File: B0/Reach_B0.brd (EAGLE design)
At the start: 107.3 x 69.5 mm, 185 parts, among them IC1 TMC2100-LA, IC10 74AHC1G126DCK, IC11 74AHC1G126DCK, IC18 74AHC1G126DCK, IC2 TMC2100-LA, IC3 74AHC1G126DCK, IC4 74AHC1G126DCK, IC5 74AHC1G126DCK, IC6 74AHC1G126DCK, IC7 74AHC1G126DCK, IC8 TMC2100-LA, IC9 74AHC1G126DCK, P8 F-2X23-, P9 F-2X23-, Q2 AON6758, Q3 AON6758, U1 SN74AHC595PW, U10 RT8268, U11 PCA9685PW, U18 CAT24C256, U2 SN74AHC595PW, U3 MCP9600, U4 MCP9600, U5 MCP9600, U6 MCP9600, U7 SN74AHC595PW, X1 22-05-7028-02, X11 22-05-7028-02, X14 22-05-7048-04, X2 MSTBA4, X21 MSTBA2, X3 MSTBA2, X4 22-05-7028-02, X5 22-05-7028-02, X6 22-05-7048-04, X7 22-05-7028-02, X8 22-05-7048-04, X9 22-05-7028-02

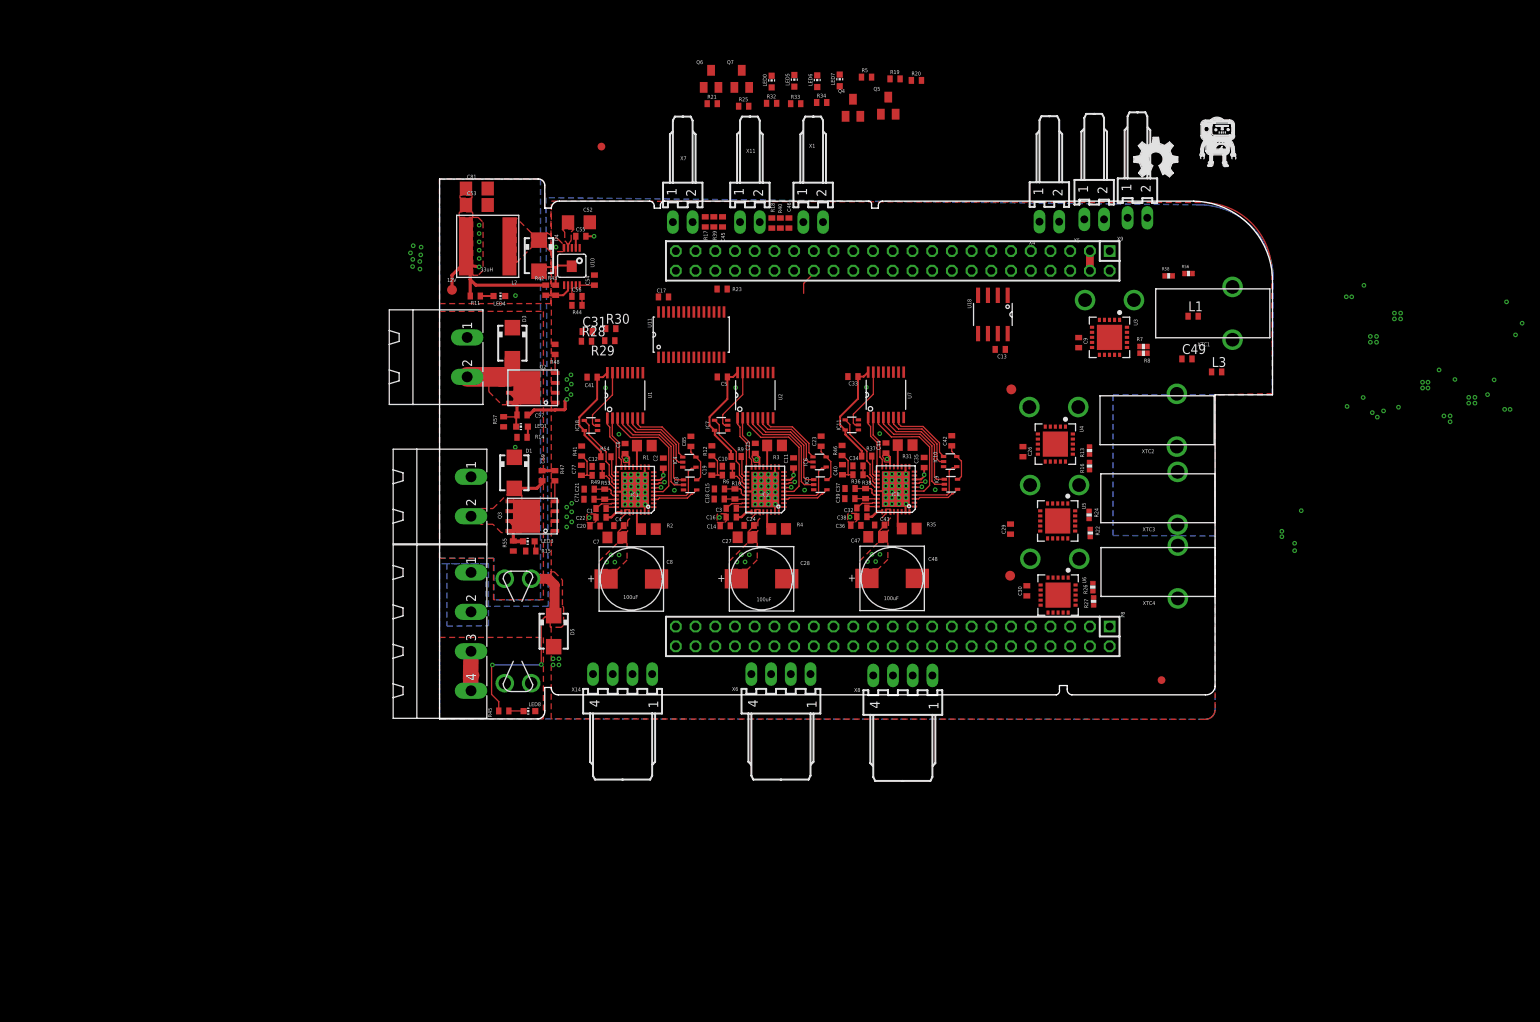
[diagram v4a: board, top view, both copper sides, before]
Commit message: thermocouple layout complete
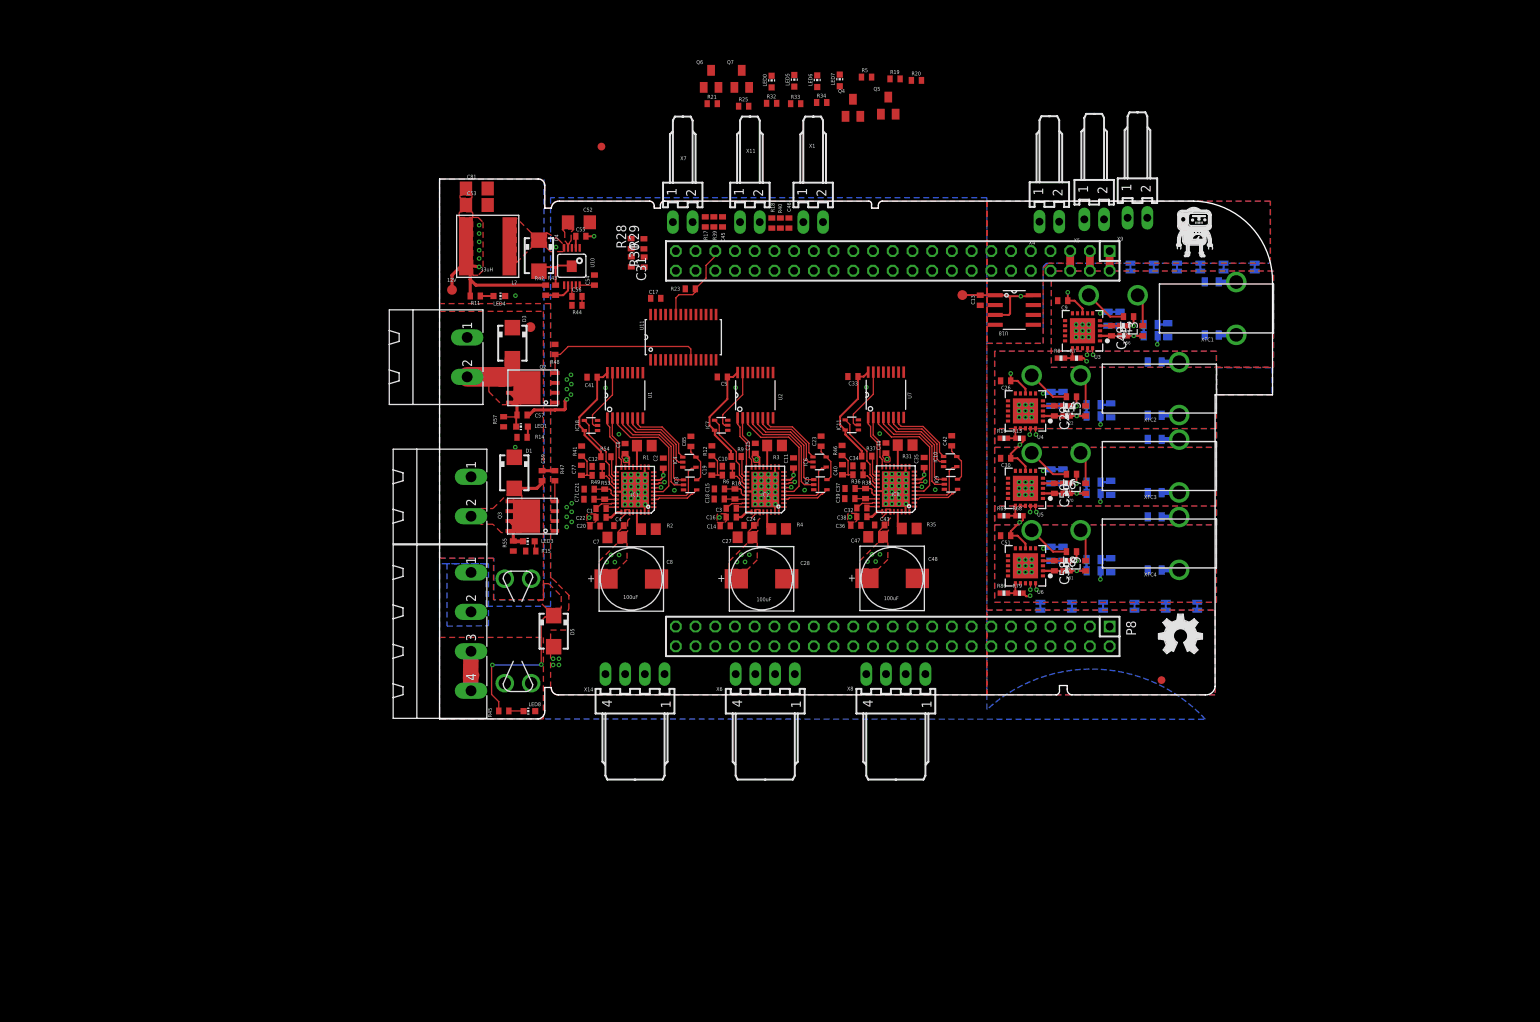
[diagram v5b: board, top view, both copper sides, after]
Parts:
- added C50, C51, C58: 0.1uF, rcl:C0402
- added JP10, JP11, JP12, JP13, JP14, JP3, JP4, JP5, JP6, JP7, JP8, JP9: (no value), SparkFun-PassivesNEW:PAD-JUMPER-2-NC_BY_TRACE_YES_SILK
- added L4, L5, L6, L7, L8, L9: BLM15HB121SN1, inductors:0402
- added R50, R51, R52, R59, R60, R63, R64, R65, R72, R73, R74, R75, R76, R83, R84, R85, R86, R87: 10k, SparkFun-Resistors:0805
- added R61, R62, R66, R67, R77, R78, R88, R89: 0, SparkFun-Resistors:0805
- added R68, R79: 10k, SparkFun-Resistors:0402-RES
- added R69: 4.3k, SparkFun-Resistors:0402-RES
- added R70, R71, R81, R82: 100, SparkFun-Resistors:0402-RES
- added R80: 7.5k, SparkFun-Resistors:0402-RES
- R22: value 10k -> 100
- R24: value 4.3k -> 100
- R26: device SparkFun-Resistors:0402-RES -> SparkFun-Resistors:0805
- R27: value 7.5k -> 10k; device SparkFun-Resistors:0402-RES -> SparkFun-Resistors:0805
- moved 12..24V 69.6 mm to (11.7, 50.5)
- moved LOGO1 61.5 mm to (92.6, 8.41)
- moved R27 26.4 mm to (80.3, 41.2), flipped to the bottom
- moved R26 24.8 mm to (78.8, 41.2), flipped to the bottom, turned to 270 degrees
- moved C30 17.3 mm to (72.9, 33.6), turned to 180 degrees
- moved C29 16.2 mm to (79.2, 39.7), turned to 270 degrees
- moved R22 15.4 mm to (80.8, 39.0), turned to 180 degrees
- moved R24 14.4 mm to (80.7, 40.3), turned to 180 degrees
- moved R28 13.8 mm to (24.7, 61.2), turned to 90 degrees
- moved 3.3V 13.7 mm to (67.3, 54.6)
- moved R29 13.2 mm to (26.3, 61.2), turned to 90 degrees
- moved U$1 12.0 mm to (96.8, 62.8)
- moved R16 11.6 mm to (72.7, 36.1), turned to 0 degrees
- moved R56 11.6 mm to (88.1, 49.4), turned to 180 degrees
- moved L3 10.9 mm to (90.6, 50.0), turned to 90 degrees
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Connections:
- removed net N$41 (its old number): U4.P$4, XTC2.P$4
- new net ENABLE_B: IC2.22, IC7.4
- new net GNDI: C26.2, C30.2, C51.2, C9.2, JP10.2, JP11.2, JP12.2, JP13.2, JP14.2, JP3.2, JP4.2, JP5.2, JP6.2, JP7.2, JP8.2, JP9.2, R16.1, R26.2, R50.2, R60.1, R61.1, R62.1, R65.1, R66.1, R67.1, R69.1, R72.2, R76.1, R77.1, R78.1, R8.1, R80.1, R83.2, R87.1, R88.1, R89.1, U3.P$1, U3.P$10, U3.P$13, U3.P$17, U3.P$18, U3.P$21, U3.P$3, U3.P$5, U3.P$6, U3.P$7, U3.P$9, U4.P$1, U4.P$10, U4.P$13, U4.P$17, U4.P$18, U4.P$21, U4.P$3, U4.P$5, U4.P$6, U4.P$7, U4.P$9, U5.P$1, U5.P$10, U5.P$13, U5.P$17, U5.P$18, U5.P$21, U5.P$3, U5.P$5, U5.P$6, U5.P$7, U5.P$9, U6.P$1, U6.P$10, U6.P$13, U6.P$17, U6.P$18, U6.P$21, U6.P$3, U6.P$5, U6.P$6, U6.P$7, U6.P$9
- new net N$123: L8.2, XTC4.P$4
- new net N$124: R79.1, R80.2, U6.P$16
- new net N$125: L9.1, R81.1, R85.2, R86.2
- new net N$126: C58.2, R81.2, U6.P$2
- new net N$128: C58.1, R82.2, U6.P$4
- new net N$130: L9.2, XTC4.P$3
- new net N$131: L8.1, R82.1, R84.1
- new net N$132: R83.1, R84.2
- new net N$133: R86.1, R87.2
- new net N$134: R88.2, XTC4.P$1
- new net N$135: R89.2, XTC4.P$2
- new net N$42: L5.1, R22.1, R63.2, R64.2
- new net N$51: R61.2, XTC1.P$1
- new net N$73: R62.2, XTC1.P$2
- new net N$75: R59.1, R60.2
- new net N$76: R66.2, XTC2.P$1
- new net N$77: R67.2, XTC2.P$2
- new net N$87: L6.2, XTC3.P$4
- new net N$88: R68.1, R69.2, U5.P$16
- new net N$89: L7.1, R70.1, R74.2, R75.2
- new net N$9: R50.1, R51.2
- new net N$90: C50.2, R70.2, U5.P$2
- new net N$91: C50.1, R71.2, U5.P$4
- new net N$92: L7.2, XTC3.P$3
- new net N$93: L6.1, R71.1, R73.1
- new net N$94: R72.1, R73.2
- new net N$95: R75.1, R76.2
- new net N$97: R77.2, XTC3.P$1
- new net N$98: R78.2, XTC3.P$2
- net +3V3: now also C51.1, R52.1, R63.1, R68.2, R74.1, R79.2, R85.1; no longer C29.1, R22.2, R26.2
- net ENABLE_A: no longer IC2.22, IC7.4
- net GND: now also JP10.1, JP11.1, JP12.1, JP13.1, JP14.1, JP3.1, JP4.1, JP5.1, JP6.1, JP7.1, JP8.1, JP9.1; no longer C26.2, C29.2, C30.2, C9.2, R16.1, R24.1, R27.1, R8.1, U3.P$1, U3.P$10, U3.P$13, U3.P$17, U3.P$18, U3.P$21, U3.P$3, U3.P$5, U3.P$6, U3.P$7, U3.P$9, U4.P$1, U4.P$10, U4.P$13, U4.P$17, U4.P$18, U4.P$21, U4.P$3, U4.P$5, U4.P$6, U4.P$7, U4.P$9, U5.P$1, U5.P$10, U5.P$13, U5.P$17, U5.P$18, U5.P$21, U5.P$3, U5.P$5, U5.P$6, U5.P$7, U5.P$9, U6.P$1, U6.P$10, U6.P$13, U6.P$17, U6.P$18, U6.P$21, U6.P$3, U6.P$5, U6.P$6, U6.P$7, U6.P$9
- net N$11: now also R52.2, R59.2
- net N$38: now also L4.2, XTC2.P$4; no longer U4.P$2, XTC2.P$3
- net N$45: now also C29.2, R22.2, U4.P$2; no longer U5.P$2, XTC3.P$3
- net N$46: now also C29.1, R24.2, U4.P$4; no longer U5.P$4, XTC3.P$4
- net N$47: now also L5.2, XTC2.P$3; no longer R22.1, R24.2, U5.P$16
- net N$48: now also L4.1, R24.1, R27.1; no longer U6.P$2, XTC4.P$3
- net N$49: now also R26.1, R27.2; no longer U6.P$4, XTC4.P$4
- net N$50: now also R64.1, R65.2; no longer R26.1, R27.2, U6.P$16
- net N$72: now also R51.1
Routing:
- net +3V3: track 67.2 -> 274.9 mm, vias 3 -> 14
- net I2C2_SCL: track 0.00 -> 41.4 mm, vias 0 -> 4
- net I2C2_SDA: track 0.00 -> 39.0 mm, vias 0 -> 4
- net HEATER_B: track 2.41 -> 21.9 mm
- net ENABLE: track 0.00 -> 11.3 mm
- net ENABLE_B: track 0.00 -> 10.1 mm
- net ENABLE_A: track 20.1 -> 10.1 mm
- net VDD_IN: track 33.5 -> 24.5 mm, vias 23 -> 21
- net N$87: track 0.00 -> 5.61 mm
- net N$38: track 0.00 -> 5.61 mm
- net N$15: track 0.00 -> 5.61 mm
- net N$123: track 0.00 -> 5.61 mm
- net N$11: track 0.00 -> 4.67 mm, vias 0 -> 1
- net N$42: track 0.00 -> 4.67 mm, vias 0 -> 1
- net N$89: track 0.00 -> 4.67 mm, vias 0 -> 1
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- added copper zone on layer 1, net GNDI
- added copper zone on layer 16, net GNDI
- added copper zone on layer 2, net GNDI
- added copper zone on layer 3, net GNDI
- removed copper zone on layer 1, net N$74
- removed copper zone on layer 3, net VDD_ADC

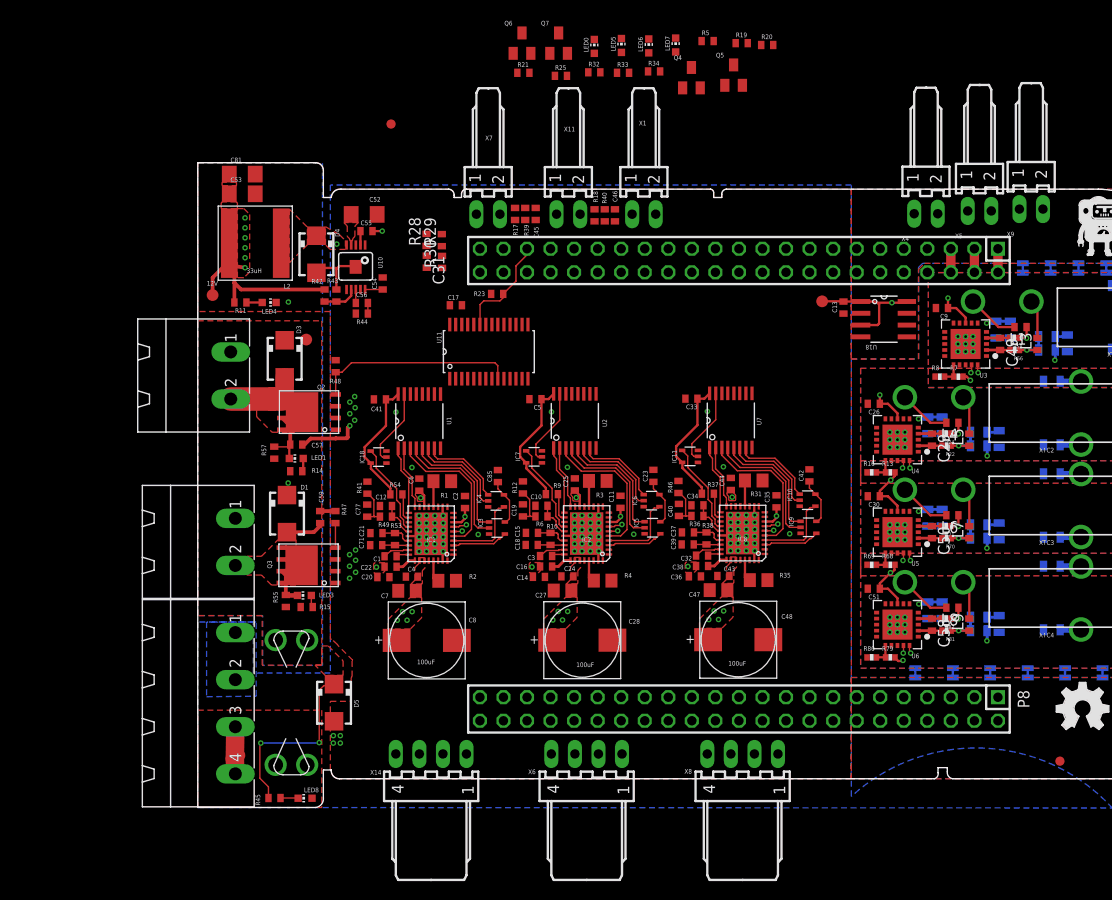
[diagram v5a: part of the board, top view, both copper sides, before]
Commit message: FETs added
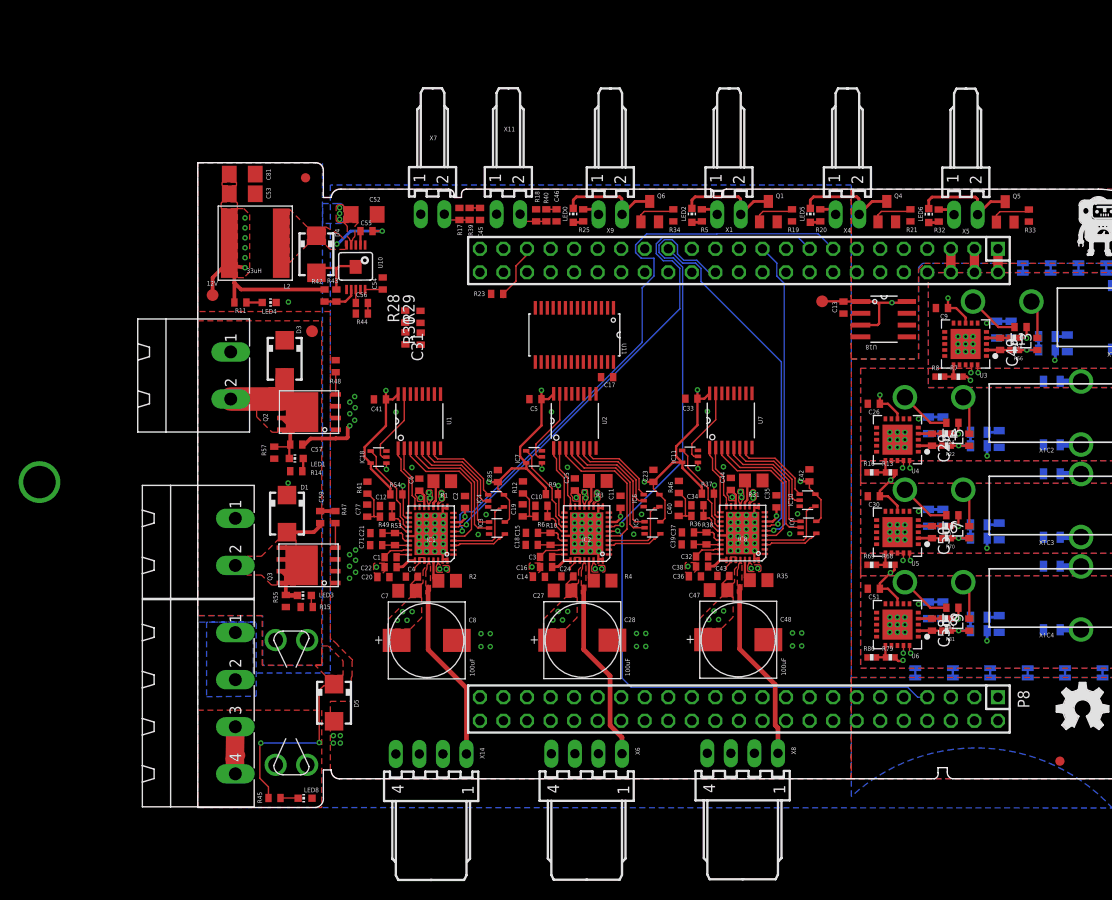
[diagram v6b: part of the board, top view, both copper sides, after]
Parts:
- removed LED7: blue, led:CHIP-LED0603
- removed Q7: (no value), semicon-smd-ipc:SOT23
- added LED2: blue, led:CHIP-LED0603
- added Q1: (no value), semicon-smd-ipc:SOT23
- moved U$4 75.1 mm to (110.5, 15.5)
- moved R33 46.4 mm to (89.7, 63.9), turned to 90 degrees
- moved X9 45.4 mm to (44.5, 64.0)
- moved R21 44.5 mm to (76.9, 63.9), turned to 90 degrees
- moved R32 40.2 mm to (79.9, 63.9), turned to 90 degrees
- moved LED6 35.3 mm to (78.8, 63.9)
- moved Q5 32.8 mm to (87.1, 64.2)
- moved LED5 27.4 mm to (66.1, 63.9)
- moved Q4 25.6 mm to (74.3, 64.3)
- moved Q6 22.8 mm to (48.8, 64.3)
- moved R19 19.4 mm to (64.1, 63.9), turned to 90 degrees
- moved R20 19.2 mm to (67.2, 63.9), turned to 90 degrees
- moved R5 18.8 mm to (54.4, 63.9), turned to 90 degrees
- moved LED0 18.4 mm to (40.5, 63.9)
- moved C17 18.1 mm to (44.2, 46.4), turned to 180 degrees
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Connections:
- net IREF_X renamed IREF_A
- net IREF_X1 renamed IREF_B
- net IREF_X2 renamed IREF_C
- net X_A3 renamed B_A3
- net X_A4 renamed B_A4
- net X_A5 renamed C_A3
- net X_A6 renamed C_A4
- net X_B3 renamed B_B3
- net X_B4 renamed B_B4
- net X_B5 renamed C_B3
- net X_B6 renamed C_B4
- removed net N$114: LED7.C, Q5.3, X1.2
- removed net N$115: LED6.C, Q4.3, X5.2
- removed net N$116: LED5.C, Q7.3, X4.2
- removed net N$117: LED6.A, R20.1
- removed net N$118: LED7.A, R21.1
- new net N$78: LED2.A, R5.1
- new net N$79: LED5.C, Q4.3, X4.2
- new net N$80: LED5.A, R20.1
- new net N$81: LED6.C, Q5.3, X5.2
- new net N$82: LED6.A, R32.1
- new net N$900: U7.9
- net FAN5: now also Q1.1, R19.2; no longer Q7.1, R33.2
- net FAN6: now also R21.2; no longer R32.2
- net FAN7: now also R33.2; no longer R5.2
- net GND: now also Q1.2, R19.1, R21.1; no longer Q7.2, R32.1, R5.1
- net N$12: now also LED2.C, Q1.3, X1.2; no longer LED5.A, R19.1
- net VDD_12V: now also R32.2, R5.2; no longer R19.2, R21.2
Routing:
- net STEP_A: track 0.97 -> 65.3 mm
- net DIR_A: track 1.49 -> 60.4 mm
- net STEP_B: track 0.97 -> 50.8 mm
- net DIR_B: track 1.49 -> 44.3 mm
- net FAULT_X: track 9.03 -> 45.8 mm, vias 0 -> 3
- net TRISTATE_STEPPERS: track 0.00 -> 36.3 mm, vias 0 -> 3
- net DIR_C: track 1.49 -> 37.2 mm
- net B_B3: track 0.00 -> 32.4 mm, vias 0 -> 2
- net X_B2: track 0.00 -> 32.2 mm, vias 0 -> 2
- net STEP_C: track 0.97 -> 33.1 mm
- net C_B3: track 0.00 -> 32.1 mm, vias 0 -> 2
- net C_B4: track 0.00 -> 31.2 mm, vias 0 -> 2
- net B_B4: track 0.00 -> 31.2 mm, vias 0 -> 2
- net X_B1: track 0.00 -> 30.8 mm, vias 0 -> 2
- net +3V3: track 274.9 -> 303.6 mm, vias 14 -> 20
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- added copper zone on layer 1, net B_A3
- added copper zone on layer 1, net B_A4
- added copper zone on layer 1, net B_B3
- added copper zone on layer 1, net B_B4
- added copper zone on layer 1, net C_A3
- added copper zone on layer 1, net C_A4
- added copper zone on layer 1, net C_B3
- added copper zone on layer 1, net C_B4
- added copper zone on layer 1, net X_A1
- added copper zone on layer 1, net X_A2
- added copper zone on layer 1, net X_B1
- added copper zone on layer 1, net X_B2
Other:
- board text added: "PWM"
- board text removed: "H"
- board text removed: "Heaters"
- board text removed: "Power"

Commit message: Add files via upload
Changed pinout to make layout simpler
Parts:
- moved U$4 44.6 mm to (119.1, 59.2)
- moved LOGO1 35.3 mm to (100.9, 42.7)
- moved U$1 25.2 mm to (116.3, 46.8)
- moved R23 9.88 mm to (36.1, 46.3)
- moved C31 3.67 mm to (25.3, 52.9)
- moved C17 3.24 mm to (46.6, 48.5), turned to 90 degrees
- moved 3.3V 0.97 mm to (67.2, 53.6)
- moved R30 0.74 mm to (24.6, 51.1), turned to 180 degrees
- moved C13 0.35 mm to (69.7, 53.6)
- moved R28 0.30 mm to (22.7, 52.9), turned to 270 degrees
- moved U18 0.29 mm to (74.1, 52.4)
- turned R17 to 270 degrees
- turned C45 to 90 degrees
- turned C46 to 90 degrees
- turned R18 to 270 degrees
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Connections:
- net DIR_A: now also P9.29; no longer P9.17
- net DIR_B: now also P9.21; no longer P9.26
- net DIR_C: now also P9.17; no longer P9.29
- net HEATER_A: now also U11.9; no longer U11.11
- net HEATER_B: now also U11.11; no longer U11.9
- net SPI1_CS0: now also P9.27
- net STEP_A: now also P9.26; no longer P9.15
- net STEP_C: now also P9.15; no longer P9.21
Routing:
- net FAN7: track 4.63 -> 62.4 mm
- net FAN6: track 4.63 -> 50.9 mm
- net VDD_5V: track 2.54 -> 47.9 mm, vias 0 -> 1
- net HEATER_A: track 2.64 -> 45.0 mm
- net SPI1_CS0: track 0.00 -> 37.5 mm, vias 0 -> 2
- net SPI1_MOSI: track 0.00 -> 37.2 mm, vias 0 -> 1
- net SPI1_SCLK: track 0.00 -> 37.0 mm, vias 0 -> 1
- net FAN5: track 4.63 -> 38.6 mm
- net HEATER_B: track 2.41 -> 29.1 mm
- net IREF_A_RAW: track 0.00 -> 26.6 mm, vias 0 -> 2
- net +3V3: track 303.6 -> 330.0 mm
- net VDD_ADC: track 0.00 -> 24.8 mm, vias 0 -> 2
- net FAULT_REACH: track 0.00 -> 22.1 mm
- net IREF_C_RAW: track 0.00 -> 18.8 mm, vias 0 -> 2
- net FAN4: track 4.63 -> 20.4 mm
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- added copper zone on layer 3, net VDD_12V
